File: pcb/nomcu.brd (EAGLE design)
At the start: 66 x 70 mm, 35 parts, among them IC4 MY_7905DT, J1 ATX24RH

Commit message: working on daughterboard
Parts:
- removed JP16: (no value), appleii:1X04
- added JP2: (no value), pinhead:1X04
- JP3: device pinhead:2X03 -> pinhead:2X04
- moved JP8 10.9 mm to (37.5, 58.9)
- moved U$4 0.36 mm to (46.4, 47.5)
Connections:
- removed net N$2: JP16.4, JP8.4
- net F12V: no longer JP16.2
- net GND: no longer JP16.1
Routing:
- net F12V: track 30.6 -> 12.2 mm
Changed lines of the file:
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@@
 <element name="U$7" library="atx_power_control" package="FUSE_HOLDER_3IN1" value="CAR_FUSE_HOLDER3IN1" x="31.496" y="37.211" smashed="yes"/>
 <element name="U$8" library="atx_power_control" package="FUSE_HOLDER_3IN1" value="CAR_FUSE_HOLDER3IN1" x="31.496" y="44.704" smashed="yes"/>
-<element name="U$4" library="396_conn" package="396_7P" value="VH396" x="46.101" y="47.244" smashed="yes" rot="R90"/>
+<element name="U$4" library="396_conn" package="396_7P" value="VH396" x="46.355" y="47.498" smashed="yes" rot="R90"/>
 <element name="R22" library="atx_power_control" package="0805" value="5K1" x="62.738" y="22.225" smashed="yes" rot="R270">
 <attribute name="NAME" x="-34.8615" y="-40.386" size="0.8128" layer="25" rot="R270"/>
 </element>
 <element name="U$9" library="atx4vc" package="WAGO257-7" value="WAGO257-7" x="56.388" y="43.382" smashed="yes" rot="R90"/>
-<element name="JP8" library="appleii" package="1X04" value="" x="26.543" y="59.182" smashed="yes" rot="R180"/>
-<element name="JP16" library="appleii" package="1X04" value="" x="36.957" y="59.182" smashed="yes" rot="R180"/>
+<element name="JP8" library="appleii" package="1X04" value="" x="37.465" y="58.928" smashed="yes" rot="R180"/>
 <element name="J4" library="SparkFun-Connectors" package="USB-C-16P" value="" x="58.166" y="15.113" smashed="yes" rot="R90">
 <attribute name="PROD_ID" value="CONN-14122" x="57.912" y="15.113" size="1.778" layer="27" rot="R90" display="off"/>
 <attribute name="VALUE" x="61.976" y="15.113" size="0.762" layer="27" rot="R90" align="center"/>
 </element>
-<element name="JP3" library="pinhead" library_urn="urn:adsk.eagle:library:325" package="2X03" package3d_urn="urn:adsk.eagle:package:22462/2" value="" x="30.988" y="29.718" smashed="yes">
-<attribute name="POPULARITY" value="62" x="30.988" y="29.718" size="1.778" layer="27" display="off"/>
+<element name="JP3" library="pinhead" library_urn="urn:adsk.eagle:library:325" package="2X04" package3d_urn="urn:adsk.eagle:package:22461/2" value="" x="30.988" y="29.718" smashed="yes">
+<attribute name="POPULARITY" value="47" x="30.988" y="29.718" size="1.778" layer="27" display="off"/>
 <attribute name="VALUE" x="27.178" y="25.273" size="1.27" layer="27"/>
+</element>
+<element name="JP2" library="pinhead" library_urn="urn:adsk.eagle:library:325" package="1X04" package3d_urn="urn:adsk.eagle:package:22407/2" value="" x="26.67" y="58.674" smashed="yes">
+<attribute name="POPULARITY" value="91" x="26.67" y="58.674" size="1.778" layer="27" display="off"/>
+<attribute name="VALUE" x="21.59" y="55.499" size="1.27" layer="27"/>
 </element>
 </elements>
@@
 <contactref element="U$9" pad="P$8"/>
 <contactref element="U$9" pad="P$7"/>
-<contactref element="JP16" pad="1"/>
 <contactref element="JP8" pad="1"/>
 <contactref element="J4" pad="SHLD2" route="any" routetag="J1.SHLD"/>
@@
 <contactref element="U$4" pad="P$7"/>
 <wire x1="32.131" y1="66.537" x2="35.306" y2="66.41" width="0" layer="19" extent="1-1"/>
-<wire x1="30.353" y1="59.182" x2="32.131" y2="66.537" width="0" layer="19" extent="1-1"/>
+<wire x1="41.275" y1="58.928" x2="35.306" y2="66.41" width="0" layer="19" extent="1-1"/>
 <wire x1="64.328" y1="24.799" x2="64.709" y2="28.228" width="0" layer="19" extent="1-1"/>
-<wire x1="19.514" y1="58.1" x2="30.353" y2="59.182" width="0" layer="19" extent="1-1"/>
+<wire x1="19.514" y1="58.1" x2="32.131" y2="66.537" width="0" layer="19" extent="1-1"/>
 <wire x1="18.415" y1="76.454" x2="32.131" y2="66.537" width="0" layer="19" extent="1-1"/>
 <wire x1="19.514" y1="37.1" x2="19.514" y2="58.1" width="0" layer="19" extent="1-1"/>
@@
 <contactref element="U$9" pad="P$1"/>
 <wire x1="53.888" y1="28.382" x2="58.888" y2="28.382" width="0" layer="19" extent="1-1"/>
+<wire x1="46.355" y1="35.618" x2="53.888" y2="28.382" width="0" layer="19" extent="1-1"/>
+<wire x1="41.188" y1="28.956" x2="46.355" y2="35.618" width="0" layer="19" extent="1-1"/>
 <wire x1="63.82" y1="19.166" x2="58.888" y2="28.382" width="0" layer="19" extent="1-1"/>
-<wire x1="46.101" y1="35.364" x2="53.888" y2="28.382" width="0" layer="19" extent="1-1"/>
-<wire x1="41.188" y1="28.956" x2="46.101" y2="35.364" width="0" layer="19" extent="1-1"/>
 <wire x1="19.514" y1="16.1" x2="41.188" y2="28.956" width="0" layer="19" extent="1-1"/>
 </signal>
@@
 <wire x1="53.888" y1="33.382" x2="58.888" y2="33.382" width="0" layer="19" extent="1-1"/>
 <wire x1="48.488" y1="31.236" x2="53.888" y2="33.382" width="0" layer="19" extent="1-1"/>
-<wire x1="46.101" y1="39.324" x2="48.488" y2="31.236" width="0" layer="19" extent="1-1"/>
+<wire x1="46.355" y1="39.578" x2="48.488" y2="31.236" width="0" layer="19" extent="1-1"/>
 </signal>
 <signal name="N$8">
@@
 <wire x1="38.546" y1="46.454" x2="38.546" y2="42.954" width="2.54" layer="16"/>
 <contactref element="U$4" pad="P$4"/>
-<wire x1="46.101" y1="47.244" x2="41.529" y2="47.244" width="2.54" layer="16"/>
+<wire x1="46.355" y1="47.498" x2="41.783" y2="47.498" width="2.54" layer="16"/>
 <wire x1="38.546" y1="44.261" x2="38.546" y2="42.954" width="2.54" layer="16"/>
-<wire x1="41.529" y1="47.244" x2="38.546" y2="44.261" width="2.54" layer="16"/>
+<wire x1="41.783" y1="47.498" x2="38.546" y2="44.261" width="2.54" layer="16"/>
 <wire x1="58.888" y1="48.382" x2="63.566" y2="49.564" width="0" layer="19" extent="1-1"/>
 <wire x1="53.888" y1="48.382" x2="58.888" y2="48.382" width="0" layer="19" extent="1-1"/>
-<wire x1="46.101" y1="47.244" x2="53.888" y2="48.382" width="0" layer="19" extent="1-1"/>
+<wire x1="46.355" y1="47.498" x2="53.888" y2="48.382" width="0" layer="19" extent="1-1"/>
 <wire x1="62.738" y1="21.325" x2="58.888" y2="48.382" width="0" layer="19" extent="1-1"/>
 <wire x1="64.77" y1="21.579" x2="62.738" y2="21.325" width="0" layer="19" extent="1-1"/>
@@
 <contactref element="U$9" pad="P$14"/>
 <contactref element="U$9" pad="P$13"/>
-<contactref element="JP16" pad="2"/>
 <contactref element="JP8" pad="2"/>
 <wire x1="38.546" y1="53.947" x2="38.546" y2="50.447" width="2.54" layer="16"/>
 <contactref element="U$4" pad="P$5"/>
-<wire x1="46.101" y1="51.204" x2="39.303" y2="51.204" width="2.54" layer="16"/>
-<wire x1="39.303" y1="51.204" x2="38.546" y2="50.447" width="2.54" layer="16"/>
-<wire x1="38.227" y1="59.182" x2="38.227" y2="54.266" width="1.016" layer="16"/>
+<wire x1="46.355" y1="51.458" x2="39.557" y2="51.458" width="2.54" layer="16"/>
+<wire x1="39.557" y1="51.458" x2="38.546" y2="50.447" width="2.54" layer="16"/>
 <wire x1="38.227" y1="54.266" x2="38.546" y2="53.947" width="1.016" layer="16"/>
-<wire x1="27.813" y1="59.182" x2="27.813" y2="57.531" width="1.016" layer="16"/>
-<wire x1="31.397" y1="53.947" x2="38.546" y2="53.947" width="1.016" layer="16"/>
-<wire x1="27.813" y1="57.531" x2="31.397" y2="53.947" width="1.016" layer="16"/>
 <wire x1="58.888" y1="58.382" x2="63.312" y2="57.692" width="0" layer="19" extent="1-1"/>
 <wire x1="53.888" y1="58.382" x2="58.888" y2="58.382" width="0" layer="19" extent="1-1"/>
-<wire x1="46.101" y1="51.204" x2="53.888" y2="58.382" width="0" layer="19" extent="1-1"/>
+<wire x1="46.355" y1="51.458" x2="53.888" y2="58.382" width="0" layer="19" extent="1-1"/>
+<wire x1="38.735" y1="58.928" x2="38.227" y2="54.266" width="0" layer="19" extent="16-16"/>
 </signal>
 <signal name="F3V3">
@@
 <wire x1="38.546" y1="38.961" x2="38.546" y2="35.461" width="2.54" layer="16"/>
 <wire x1="38.546" y1="38.961" x2="39.723" y2="38.961" width="2.54" layer="16"/>
-<wire x1="44.046" y1="43.284" x2="46.101" y2="43.284" width="2.54" layer="16"/>
-<wire x1="39.723" y1="38.961" x2="44.046" y2="43.284" width="2.54" layer="16"/>
+<wire x1="44.3" y1="43.538" x2="46.355" y2="43.538" width="2.54" layer="16"/>
+<wire x1="39.723" y1="38.961" x2="44.3" y2="43.538" width="2.54" layer="16"/>
 <wire x1="58.888" y1="38.382" x2="63.82" y2="39.971" width="0" layer="19" extent="1-1"/>
 <wire x1="53.888" y1="38.382" x2="58.888" y2="38.382" width="0" layer="19" extent="1-1"/>
-<wire x1="46.101" y1="43.284" x2="53.888" y2="38.382" width="0" layer="19" extent="1-1"/>
+<wire x1="46.355" y1="43.538" x2="53.888" y2="38.382" width="0" layer="19" extent="1-1"/>
 </signal>
 <signal name="N$17">
@@
 <wire x1="54.356" y1="17.399" x2="62.738" y2="23.125" width="0" layer="19" extent="1-1"/>
 </signal>
-<signal name="N$2">
-<contactref element="JP16" pad="4"/>
-<contactref element="JP8" pad="4"/>
-<wire x1="22.733" y1="59.182" x2="33.147" y2="59.182" width="0" layer="19" extent="1-1"/>
-</signal>
 <signal name="N$11">

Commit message: working on new version
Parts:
- removed JP5: (no value), atx_power_control:1X03
- added U$11, U$6: M3_MOUNTING_HOLE, a:M3_MOUNTING_HOLE_PACK
- JP2: device pinhead:1X04 -> pinhead:1X02
- U$9: value WAGO257-7 -> DG2204R-5.0; device atx4vc:WAGO257-7 -> atx4vc:DG2204R
- moved JP2 48.3 mm to (52.7, 18.0), turned to 180 degrees
- moved C5 14.7 mm to (50.3, 30.4)
- moved LED5 12.0 mm to (54.5, 48.5), turned to 0 degrees
- moved R4 11.3 mm to (53.6, 33.9), turned to 180 degrees
- moved R9 11.0 mm to (53.6, 39.9), turned to 0 degrees
- moved LED1 10.9 mm to (54.5, 30.9), turned to 0 degrees
- moved LED7 10.8 mm to (54.5, 42.7), turned to 0 degrees
- moved R10 10.3 mm to (53.6, 45.6), turned to 0 degrees
- moved LED4 10.2 mm to (54.5, 26.5)
- moved LED6 10.2 mm to (54.5, 37.0)
- moved R7 9.68 mm to (54.5, 22.6)
- moved R8 9.09 mm to (54.5, 52.3), turned to 270 degrees
- moved R12 7.08 mm to (59.5, 21.3), turned to 90 degrees
- moved U$9 6.44 mm to (62.7, 42.3), turned to 270 degrees
- moved JP8 5.97 mm to (31.5, 59.2)
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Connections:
- net -12V: now also U$9.P$13, U$9.P$14; no longer U$9.P$1, U$9.P$2
- net -5V: now also U$9.P$11, U$9.P$12; no longer U$9.P$3, U$9.P$4
- net F12V: now also U$9.P$5, U$9.P$6; no longer U$9.P$13, U$9.P$14
- net F3V3: now also U$9.P$10, U$9.P$9; no longer U$9.P$5, U$9.P$6
- net F5V: now also U$9.P$7, U$9.P$8; no longer U$9.P$10, U$9.P$9
- net GND: now also JP2.1, U$9.P$1, U$9.P$2, U$9.P$3, U$9.P$4; no longer JP5.3, U$9.P$11, U$9.P$12, U$9.P$7, U$9.P$8
- net N$15: now also JP2.2; no longer JP5.2
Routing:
- net -12V: track 0.00 -> 73.8 mm
- net F5V: track 14.0 -> 82.4 mm
- net -5V: track 0.00 -> 35.8 mm, vias 0 -> 1
- net F3V3: track 13.2 -> 41.0 mm
- net F12V: track 12.2 -> 38.6 mm
- net N$17: track 0.00 -> 6.27 mm
- net N$5: track 0.00 -> 3.13 mm
- net N$8: track 0.00 -> 1.99 mm
- net N$20: track 0.00 -> 1.87 mm
- net N$18: track 0.00 -> 1.87 mm
- net N$9: track 0.00 -> 1.86 mm
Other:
- board size 66 x 70 mm -> 69.4 x 70 mm
- board text added: "- +"
- board text added: "-12"
- board text added: "-5"
- board text added: "3V3"
- board text added: "5V"
- board text added: "G"
- board text added: "LED"
- board text added: "PSW"

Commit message: working on new version
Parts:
- added JP4: (no value), pinhead:2X02
- added U$12: PINHD1X4, adafruit_changed:1X04-CLEANBIG
- J1: device SparkFun-Connectors:ATX24_RIGHT_ANGLE -> nomcu:ATX24_RIGHT_ANGLE
- JP3: device pinhead:2X04 -> pinhead:2X03
- moved LED3 48.9 mm to (28.7, 22.5), turned to 270 degrees
- moved LED2 46.8 mm to (28.7, 24.9), turned to 270 degrees
- moved R3 45.0 mm to (32.6, 22.5), turned to 180 degrees
- moved R6 42.5 mm to (32.6, 24.9), turned to 180 degrees
- moved C5 7.88 mm to (42.4, 30.2)
- moved IC4 4.97 mm to (47.2, 26.3), turned to 180 degrees
- moved JP8 4.95 mm to (36.4, 59.2)
- moved U$11 3.00 mm to (34.5, 11.0)
- moved J1 0.63 mm to (8.62, 35.0)
- moved U$9 0.51 mm to (63.2, 42.3)
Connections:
- new net N$3: JP3.3, JP8.4
- new net N$4: J4.A6, J4.B6, JP4.2
- new net N$6: J4.A7, J4.B7, JP4.4
- new net N$7: JP3.4, JP4.1, JP4.3, U$12.2
- net F5V: now also U$12.1
- net GND: now also JP3.2, U$12.4
- net N$11: now also JP3.5
- net N$15: now also JP3.6
- net VCC: now also JP3.1
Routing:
- net N$11: track 0.00 -> 71.9 mm, vias 0 -> 1
- net N$7: track 0.00 -> 62.5 mm
- net GND: track 0.00 -> 56.0 mm
- net N$15: track 0.00 -> 42.7 mm
- net VCC: track 0.00 -> 41.4 mm
- net N$3: track 0.00 -> 39.6 mm
- net F5V: track 82.4 -> 101.4 mm
- net N$4: track 0.00 -> 18.2 mm
- net N$6: track 0.00 -> 16.7 mm
- net N$21: track 43.3 -> 58.0 mm
- net -5V: track 35.8 -> 46.4 mm, vias 1 -> 0
- net N$10: track 37.0 -> 45.1 mm
- net F12V: track 38.6 -> 44.8 mm
- net N$29: track 0.00 -> 1.99 mm
- net N$1: track 0.00 -> 1.99 mm
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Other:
- board text added: "5VSB"
- board text removed: "+"
- board text removed: "PWR LED"
- board text removed: "PWR SW"
- board text removed: "SB"

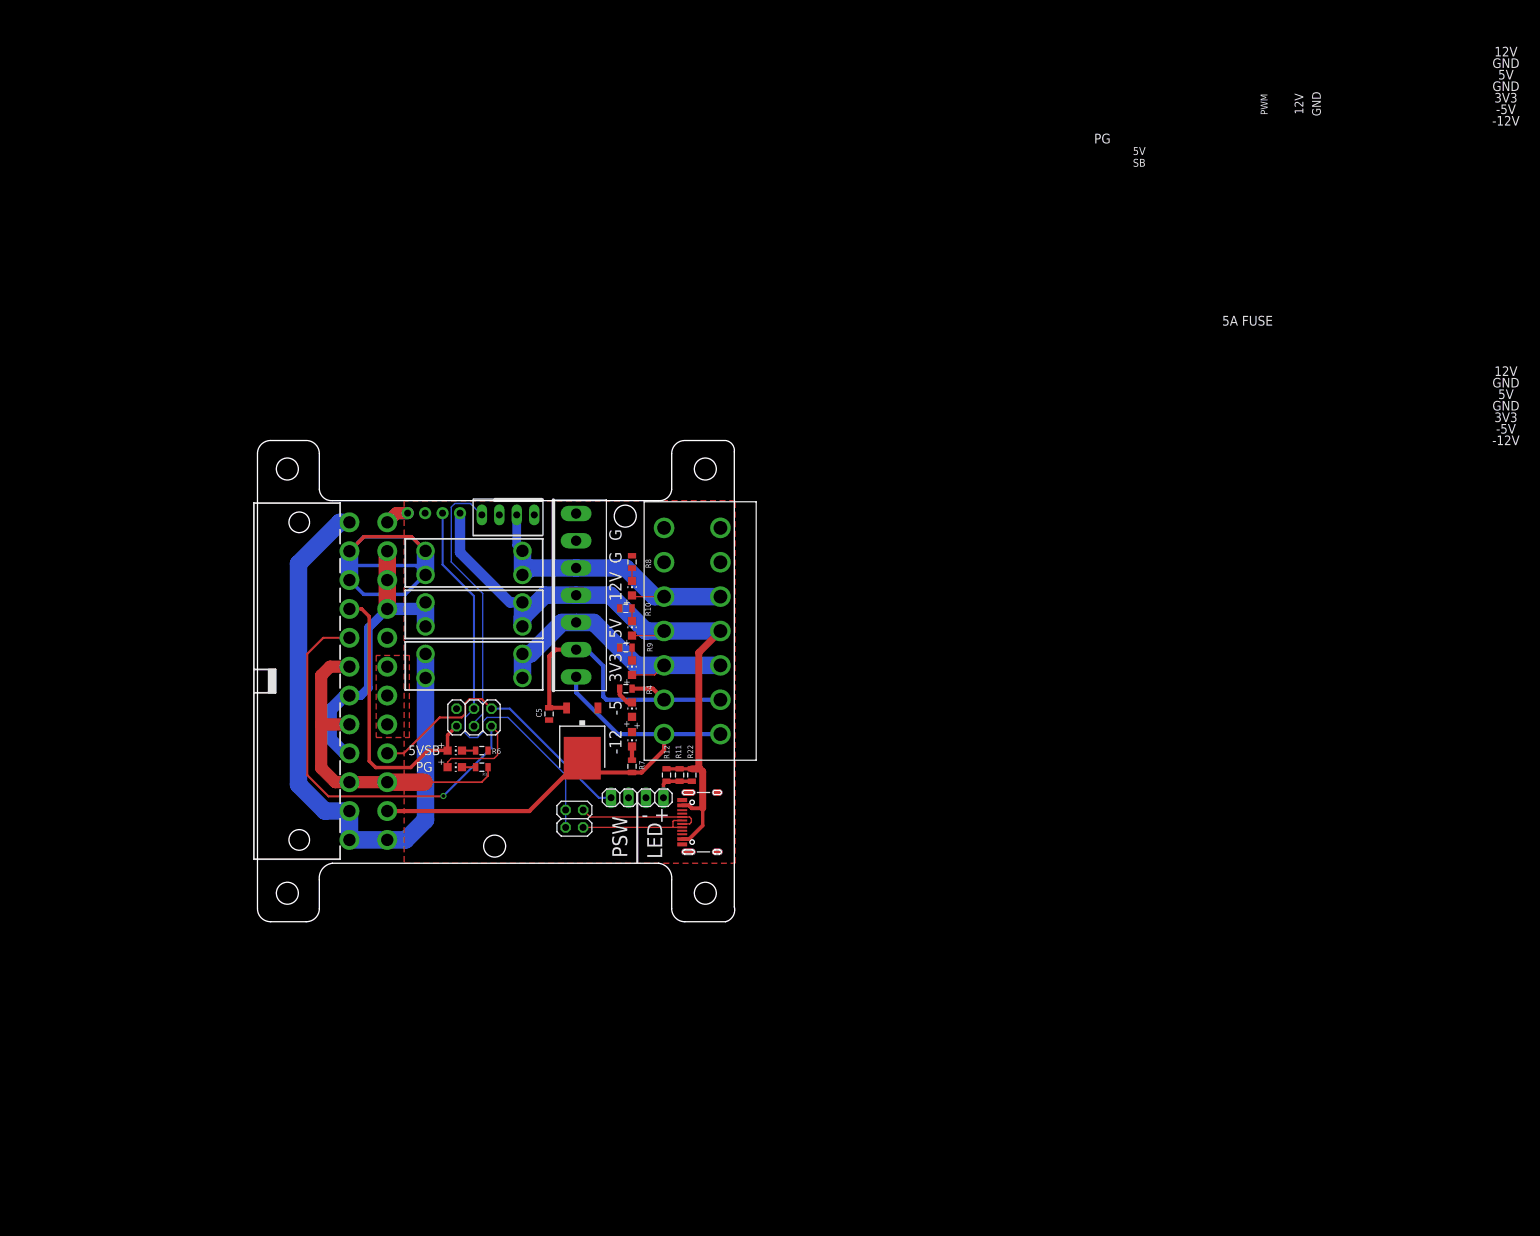
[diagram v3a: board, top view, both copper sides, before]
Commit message: new daughterboard
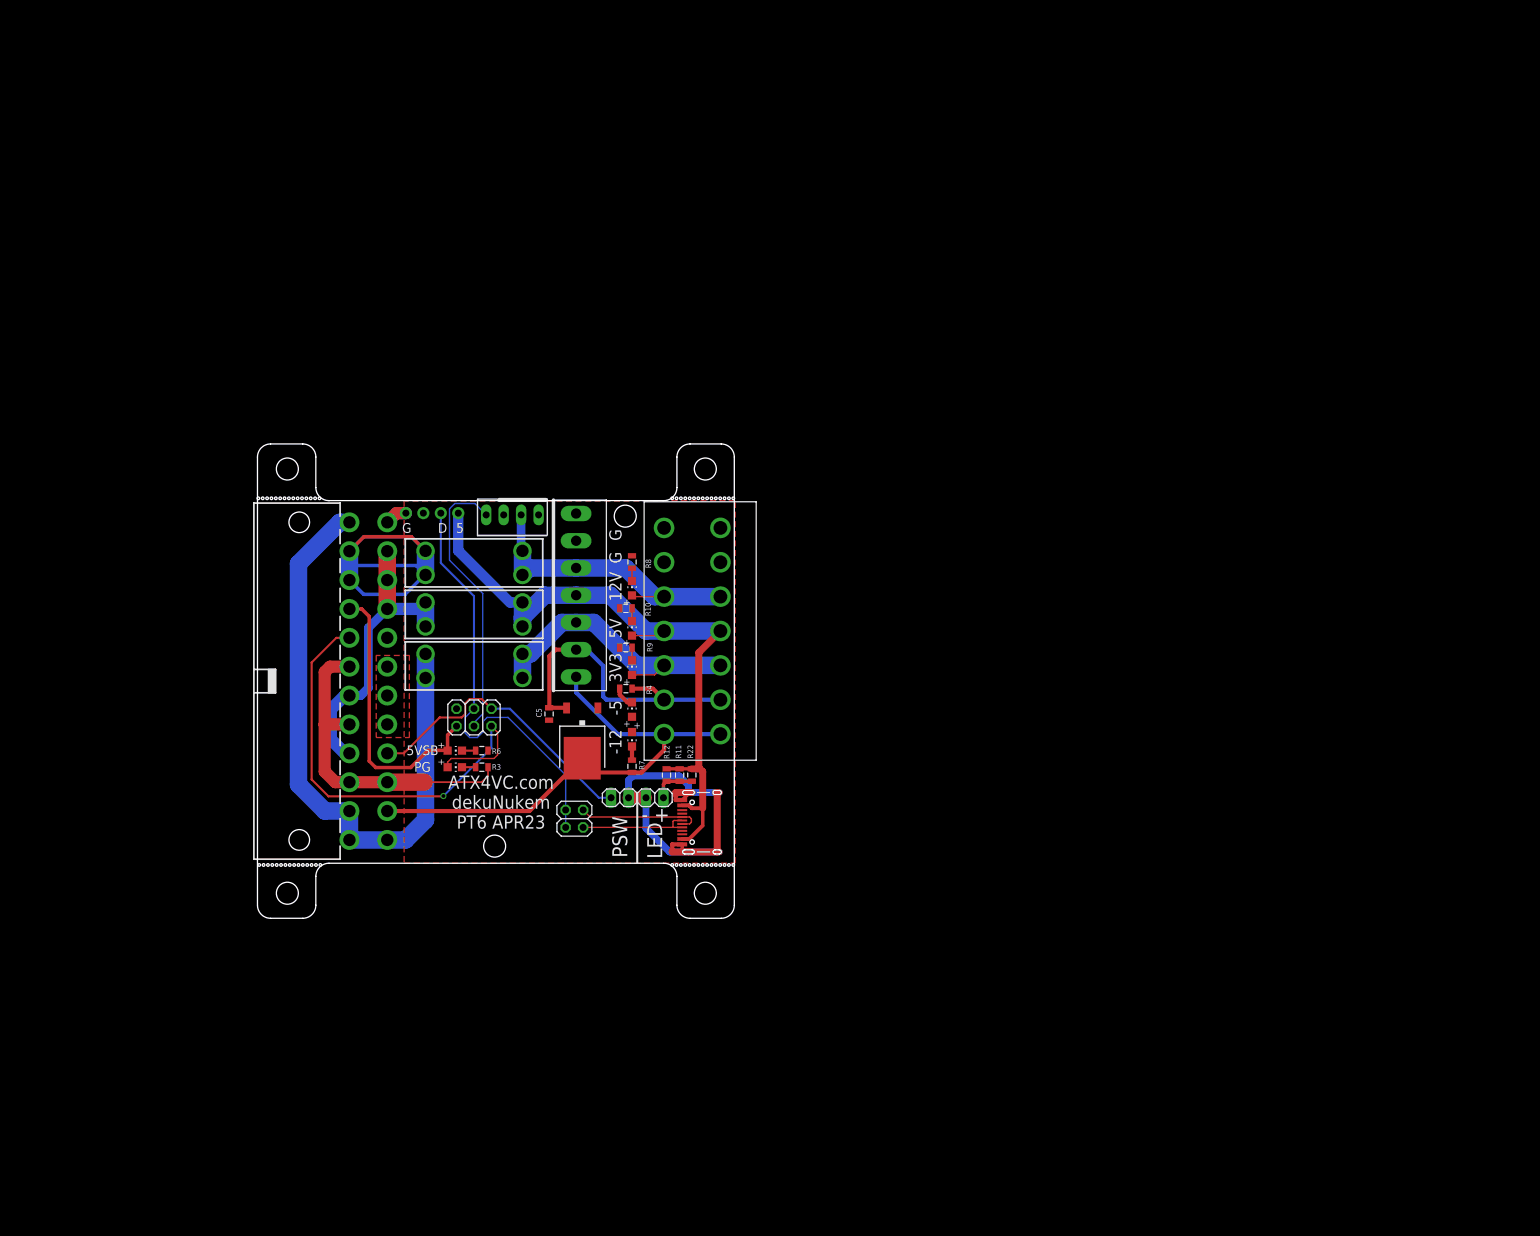
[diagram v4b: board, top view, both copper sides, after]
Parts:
- moved JP8 0.64 mm to (37.1, 59.2)
- moved U$12 0.25 mm to (25.4, 59.4)
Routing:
- net GND: track 56.0 -> 115.8 mm
- net N$11: track 71.9 -> 70.3 mm
- net N$3: track 39.6 -> 40.5 mm
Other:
- board size 69.4 x 70 mm -> 69.4 x 69 mm
- board text added: "5"
- board text added: "ATX4VC.com dekuNukem PT6 APR23"
- board text added: "D"
- board text removed: "12V GND 5V GND 3V3 -5V -12V"
- board text removed: "5A FUSE"
- board text removed: "5V SB"
- board text removed: "ATX4VC.com dekuNukem NOV 2022 PD2"
- board text removed: "GND"
- board text removed: "PWM"
